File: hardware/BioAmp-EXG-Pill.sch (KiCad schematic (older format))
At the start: 21 parts, among them J1 Conn_01x03, J2 Conn_01x03, U1 TL074

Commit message: BioaAmp EXG Pill v0.9 KiCAD schematic
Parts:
- removed C3: 100n, Capacitor_SMD:C_0603_1608Metric_Pad1.08x0.95mm_HandSolder, symbol Device:C
- added C5: 47nF, Capacitor_SMD:C_0603_1608Metric_Pad1.08x0.95mm_HandSolder, symbol Device:C
- added R10, R14, R15: 0R, Resistor_SMD:R_0201_0603Metric_Pad0.64x0.40mm_HandSolder, symbol Device:R
- added R13: 1M, Resistor_SMD:R_0603_1608Metric_Pad0.98x0.95mm_HandSolder, symbol Device:R
- C1: value 47uf -> 47uF
- C2: value 100nf -> 4.7nF
- C4: value 100n -> 2.2uF
- C7, C9: value 100nf -> 100nF
- C8: value 2.2uf -> 2.2uF
- J1: value Conn_01x03 -> BioAmp Input
- J2: value Conn_01x03 -> BioAmp Output
- R1, R4: value 82k -> 10K
- R11: value 100k -> 1k
- R12: value 100k -> 1M
- R2, R3: value 10k -> 1K
- R5: value 1k -> 1K
- R6: value 100k -> RG
- R8, R9: value 10k -> 10K
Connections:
- net labels added: IN+, IN-
- net labels removed: BIO+, BIO-, vRef
- wire segments 39 -> 60
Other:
- note added: "Electrode config"
- note added: "Electrode reference"
- note added: "Filter config"
- note added: "INA gain config"
- note added: "Instrumentation Amp"
- note added: "Power supply filtering"
- note removed: "8.2x Gain Instrumentation Amp"
- note removed: "Power Supply"
- moved on the sheet: C1, C2, C4, C7, C8, C9, J1, J2, R1, R11, R2, R3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

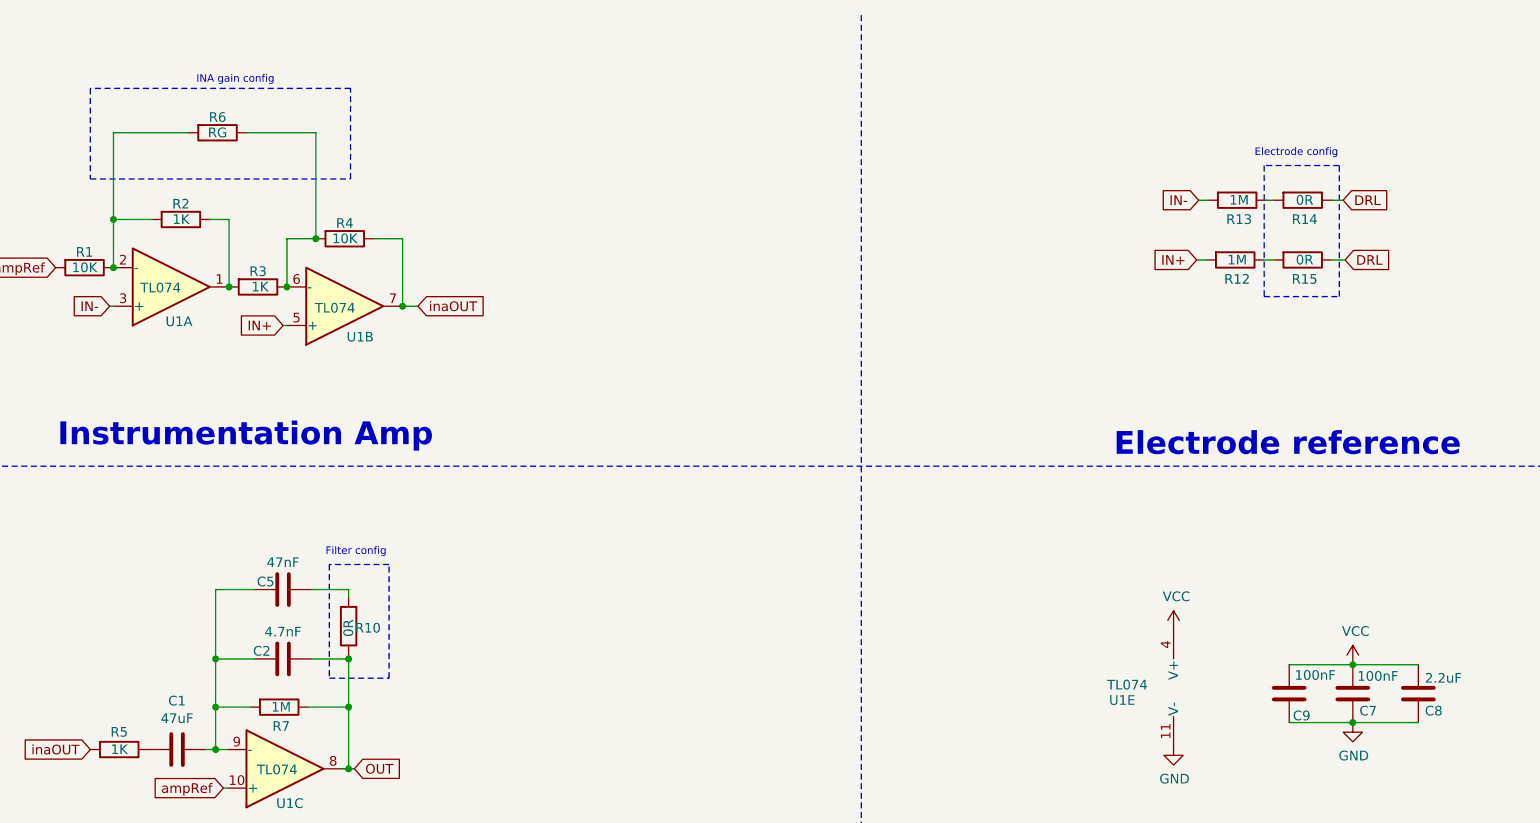
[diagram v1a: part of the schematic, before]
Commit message: Update v0.9 schematic part values
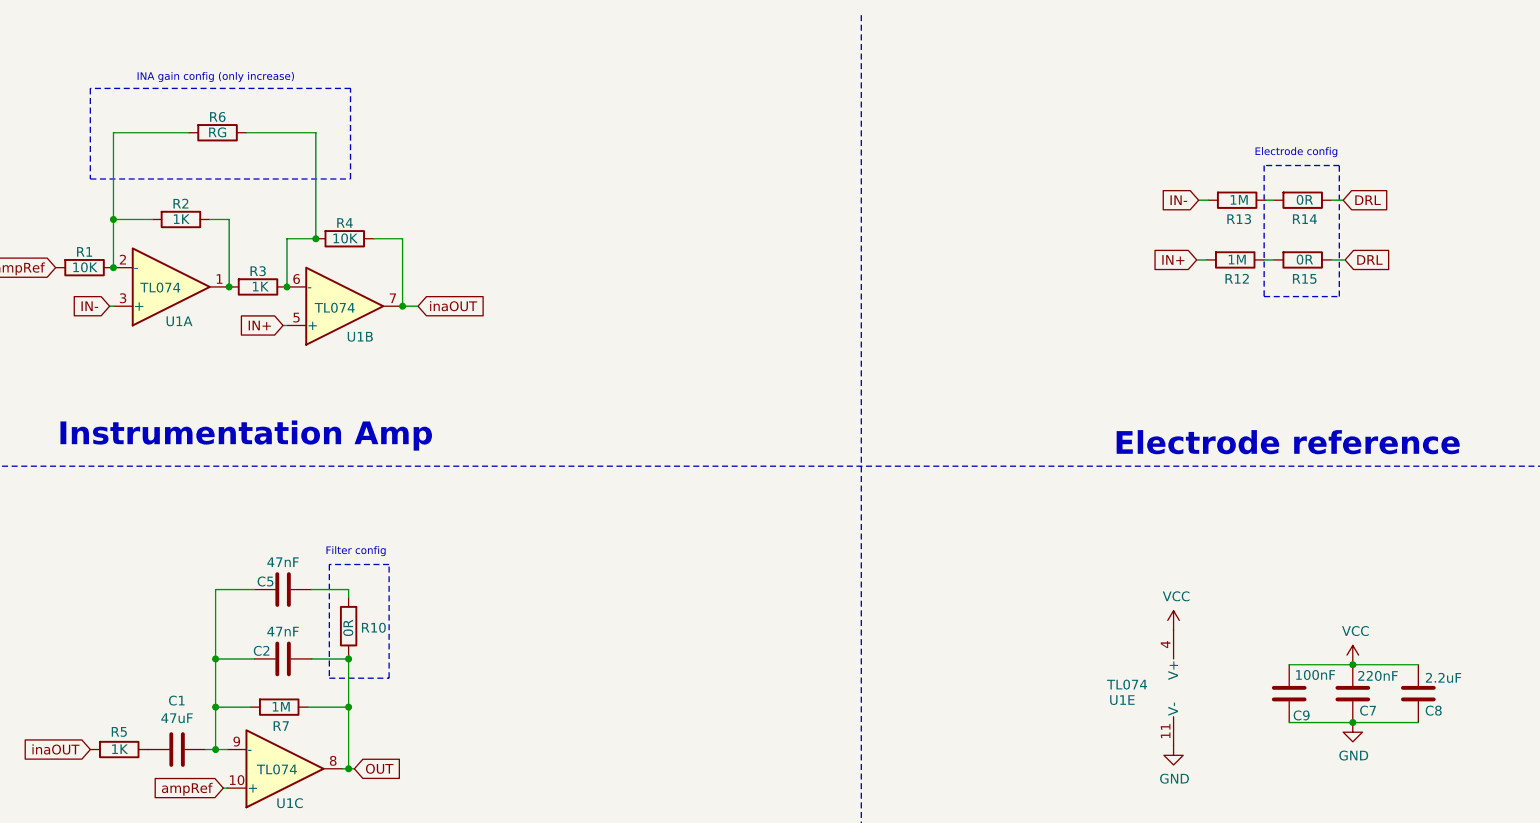
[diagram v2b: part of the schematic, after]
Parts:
- C2: value 4.7nF -> 47nF
- C7: value 100nF -> 220nF
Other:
- note added: "INA gain config (only increase)"
- note removed: "INA gain config"
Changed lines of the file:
@@
 Wire Notes Line
 	4320 850  2970 850
-Text Notes 3520 830  0    39   ~ 0
-INA gain config
+Text Notes 3210 820  0    39   ~ 0
+INA gain config (only increase)
 $Comp
 L Device:R R1
@@
 P 3970 3810
 F 0 "C2" V 4010 3700 50  0000 C CNN
-F 1 "4.7nF" V 4110 3810 50  0000 C CNN
+F 1 "47nF" V 4110 3810 50  0000 C CNN
 F 2 "Capacitor_SMD:C_0603_1608Metric_Pad1.08x0.95mm_HandSolder" H 4008 3660 50  0001 C CNN
 F 3 "~" H 3970 3810 50  0001 C CNN
@@
 U 1 1 60BD7FA4
 P 4310 3640
-F 0 "R10" H 4210 3650 50  0000 C CNN
+F 0 "R10" H 4180 3650 50  0000 C CNN
 F 1 "0R" V 4310 3650 50  0000 C CNN
 F 2 "Resistor_SMD:R_0201_0603Metric_Pad0.64x0.40mm_HandSolder" V 4240 3640 50  0001 C CNN
@@
 P 9520 3990
 F 0 "C7" H 9440 4080 50  0000 C CNN
-F 1 "100nF" H 9390 3900 50  0000 C CNN
+F 1 "220nF" H 9390 3900 50  0000 C CNN
 F 2 "Capacitor_SMD:C_0603_1608Metric_Pad1.08x0.95mm_HandSolder" H 9558 3840 50  0001 C CNN
 F 3 "~" H 9520 3990 50  0001 C CNN

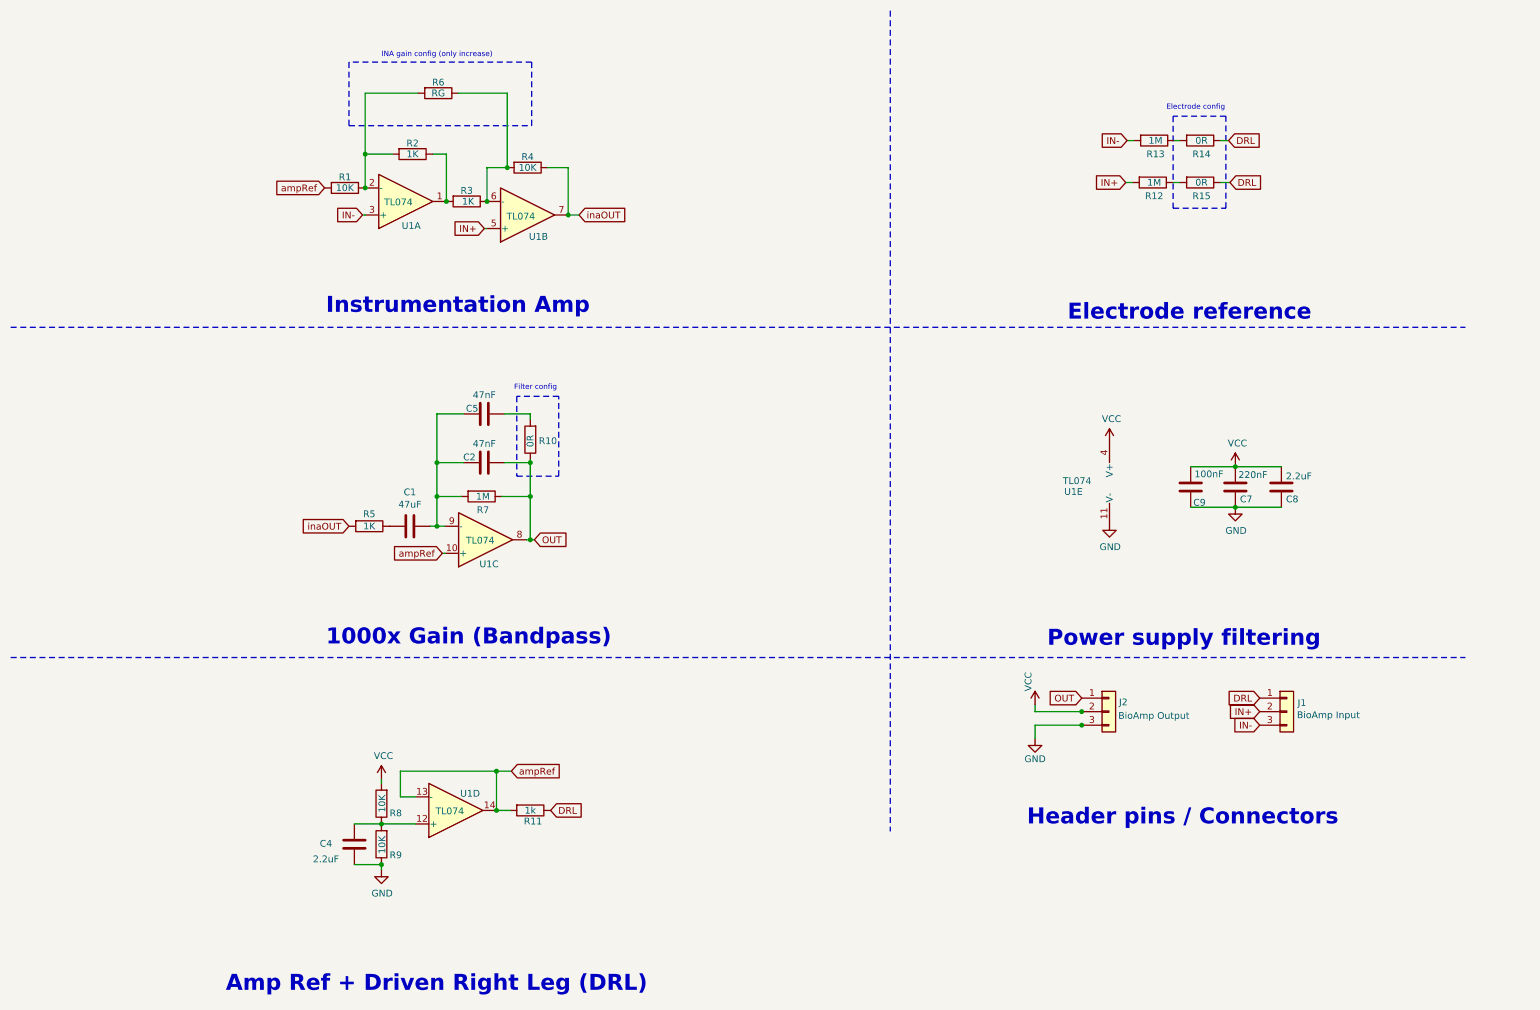
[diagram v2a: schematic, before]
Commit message: BioAmp EXG Pill v1.0 alpha schematic
This version of the BioAmp EXG Pill is near to the final release version (v1.0) for the Crowd Supply campaign.
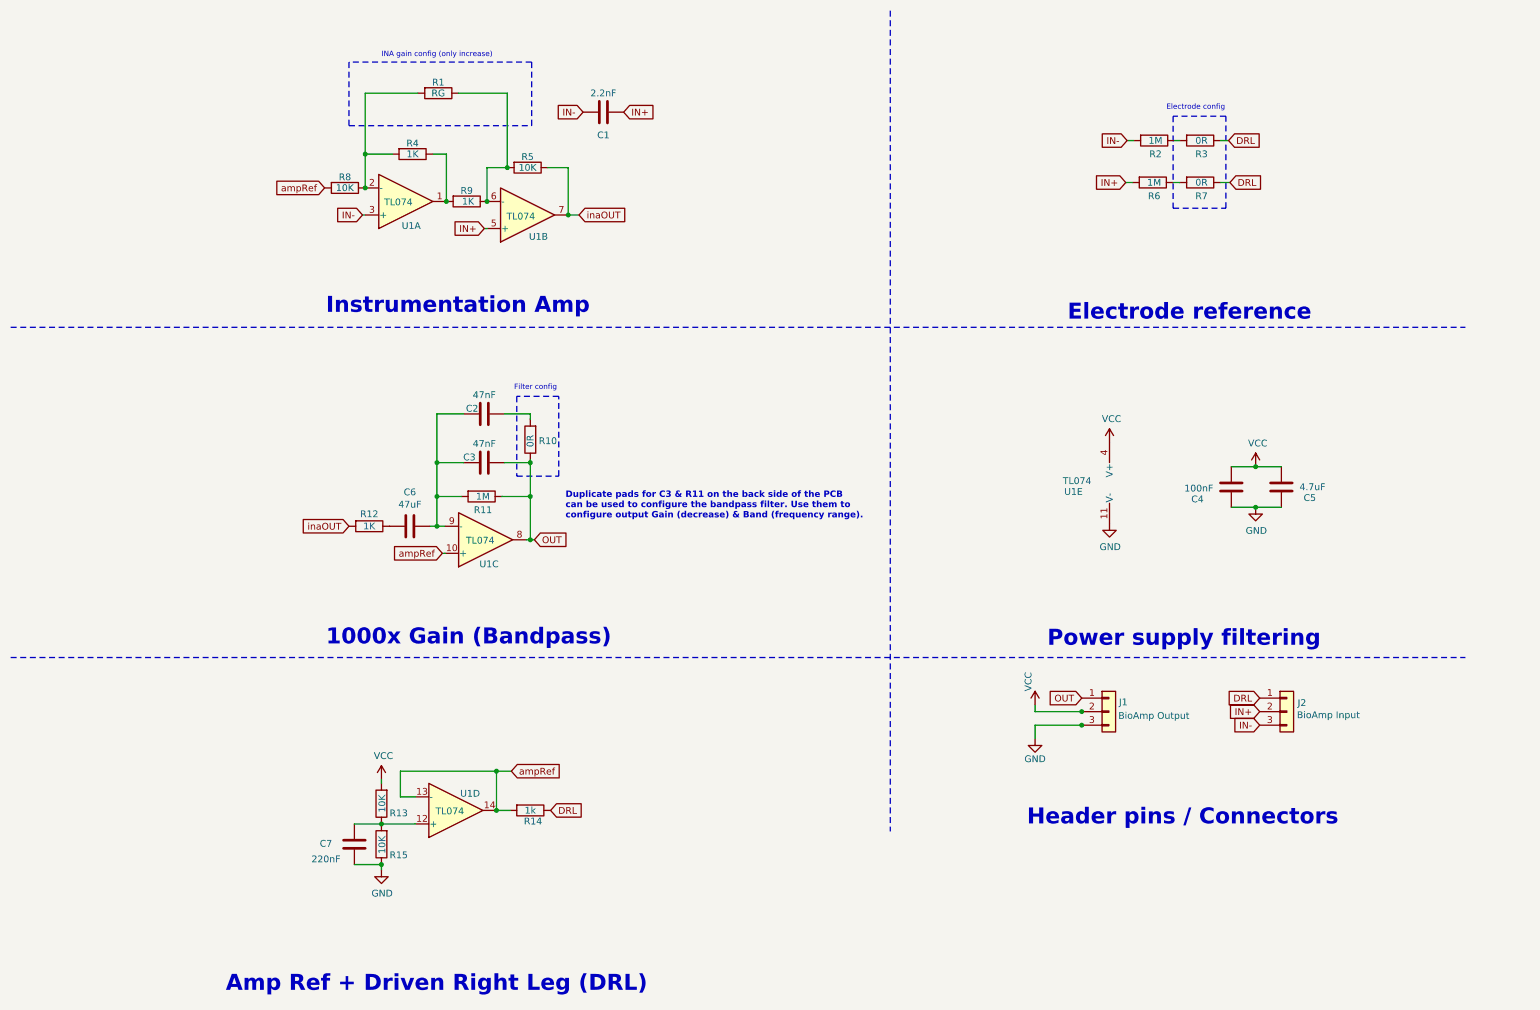
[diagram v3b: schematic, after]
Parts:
- removed C7: 220nF, Capacitor_SMD:C_0603_1608Metric_Pad1.08x0.95mm_HandSolder, symbol Device:C
- added C1: 2.2nF, Capacitor_SMD:C_0603_1608Metric_Pad1.08x0.95mm_HandSolder, symbol Device:C
- C5: renamed from C8; value 2.2uF -> 4.7uF
- C7: renamed from C4; value 2.2uF -> 220nF
- renumbered C5 to C2, C2 to C3, C9 to C4, C1 to C6, J2 to J1, J1 to J2, R6 to R1, R7 to R11, R5 to R12, R8 to R13, R11 to R14, R9 to R15, R13 to R2, R14 to R3, R2 to R4, R4 to R5, R12 to R6, R15 to R7, R1 to R8, R3 to R9
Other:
- note added: "Duplicate pads for C3 & R11 on the back side of the PCB\ncan be used to configure the bandpass filter. Use them to\nconfigure output Gain (decrease) & Band (frequency range)."
- moved on the sheet: C4

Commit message: BioAmp EXG Pill v1.0b KiCAD files
This is the Beta version of the BioAmp EXG Pill v1.0 with updated power pinout, solder jumpers and more.
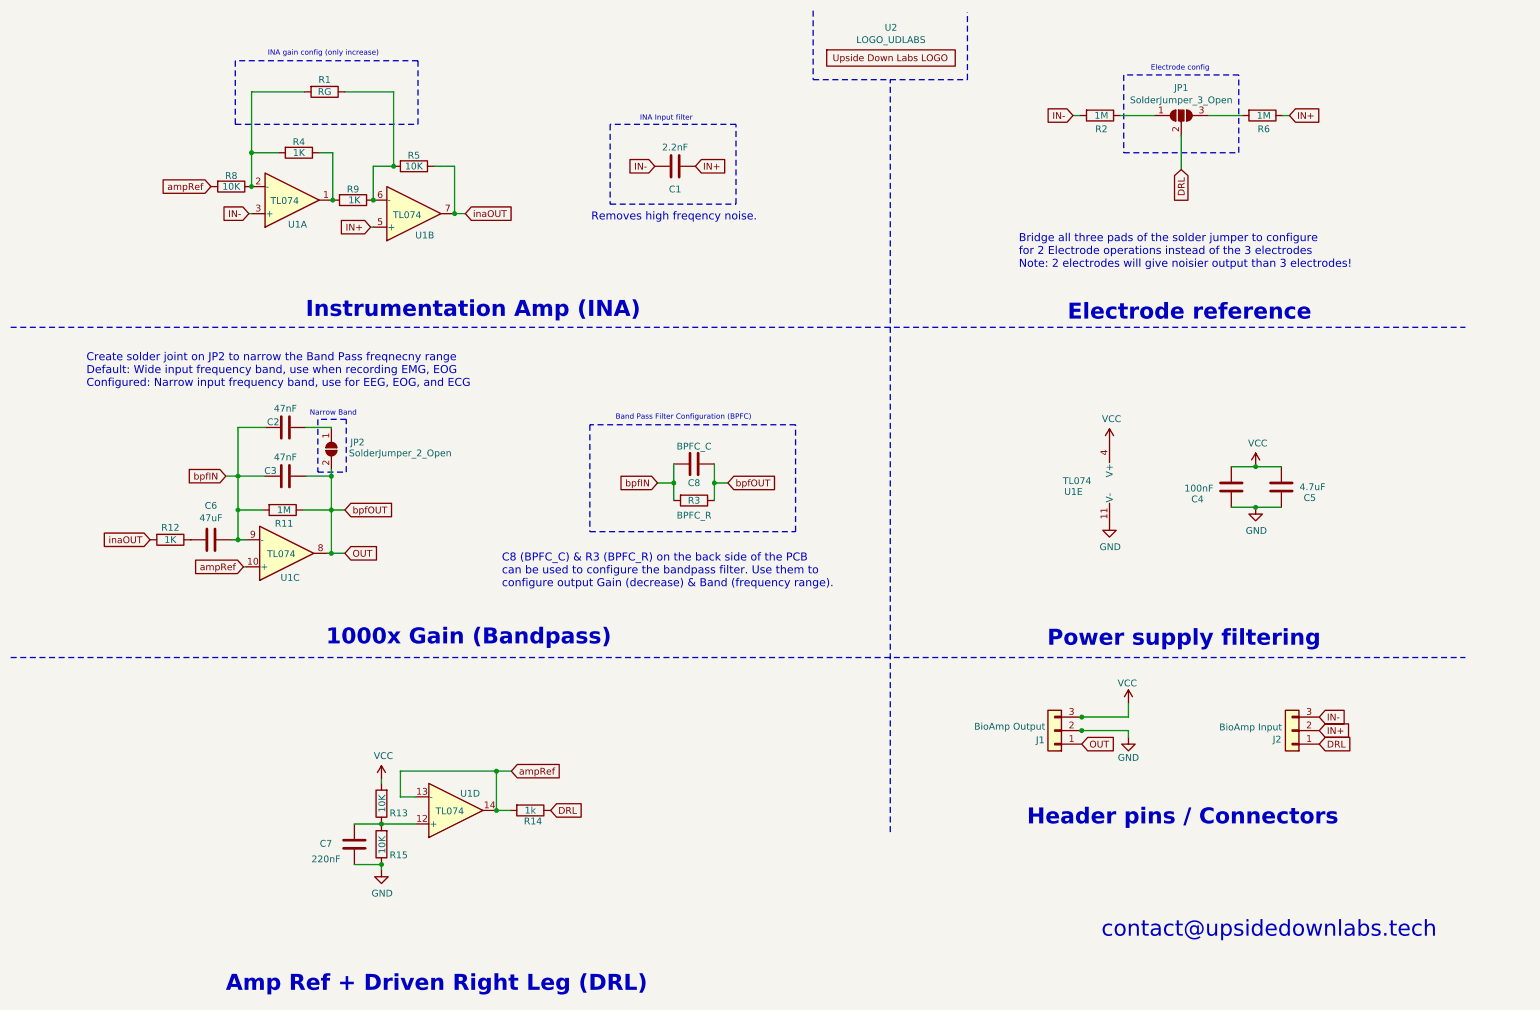
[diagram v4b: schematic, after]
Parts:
- removed R10, R7: 0R, Resistor_SMD:R_0201_0603Metric_Pad0.64x0.40mm_HandSolder, symbol Device:R
- added C8: BPFC_C, Capacitor_SMD:C_0603_1608Metric_Pad1.08x0.95mm_HandSolder, symbol Device:C
- added JP1: SolderJumper_3_Open, Jumper:SolderJumper-3_P1.3mm_Open_RoundedPad1.0x1.5mm, symbol Jumper:SolderJumper_3_Open
- added JP2: SolderJumper_2_Open, Jumper:SolderJumper-2_P1.3mm_Open_RoundedPad1.0x1.5mm, symbol Jumper:SolderJumper_2_Open
- added U2: LOGO_UDLABS, udlabs:EXG, symbol udlabs:LOGO_UDLABS
- R3: value 0R -> BPFC_R; footprint Resistor_SMD:R_0201_0603Metric_Pad0.64x0.40mm_HandSolder -> Resistor_SMD:R_0603_1608Metric_Pad0.98x0.95mm_HandSolder
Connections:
- net labels added: bpfIN, bpfOUT
- wire segments 60 -> 67
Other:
- note added: "Band Pass Filter Configuration (BPFC)"
- note added: "Bridge all three pads of the solder jumper to configure\nfor 2 Electrode operations instead of the 3 electrodes\nNote: 2 electrodes will give noisier output than 3 electrodes!"
- note added: "C8 (BPFC_C) & R3 (BPFC_R) on the back side of the PCB\ncan be used to configure the bandpass filter. Use them to\nconfigure output Gain (decrease) & Band (frequency range)."
- note added: "Create solder joint on JP2 to narrow the Band Pass freqnecny range\nDefault: Wide input frequency band, use when recording EMG, EOG\nConfigured: Narrow input frequency band, use for EEG, EOG, and ECG"
- note added: "INA Input filter"
- note added: "Instrumentation Amp (INA)"
- note added: "Narrow Band"
- note added: "Removes high freqency noise."
- note added: "contact@upsidedownlabs.tech"
- note removed: "Duplicate pads for C3 & R11 on the back side of the PCB\ncan be used to configure the bandpass filter. Use them to\nconfigure output Gain (decrease) & Band (frequency range)."
- note removed: "Filter config"
- note removed: "Instrumentation Amp"
- moved on the sheet: C1, C2, C3, C6, J1, J2, R1, R11, R12, R2, R4, R5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
